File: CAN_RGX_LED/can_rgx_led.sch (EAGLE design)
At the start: 9 parts

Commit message: board 1_0
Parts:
- added R1: 22M, SparkFun-Resistors:22MOHM-0603-1/10W-10%
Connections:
- new net N$8: R1.1, U$1.A
- net +: now also R1.2; no longer U$1.A
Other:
- moved on the sheet: U$1, U$2, U$3, U$4, U$5, U$6, U$7, U$8
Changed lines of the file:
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@@
 <part name="U$8" library="uORocketry-parts" deviceset="OSLONSSL150" device=""/>
 <part name="J1" library="SparkFun-Connectors" deviceset="CONN_02" device=""/>
+<part name="R1" library="SparkFun-Resistors" deviceset="22MOHM" device="-0603-1/10W-10%" value="22M"/>
 </parts>
 <sheets>
@@
 </plain>
 <instances>
-<instance part="U$1" gate="G$1" x="33.02" y="55.88" smashed="yes">
-<attribute name="NAME" x="32.512" y="52.451" size="1.778" layer="95" font="vector" rot="R180"/>
-<attribute name="VALUE" x="32.512" y="57.785" size="1.778" layer="96" font="vector" rot="R180" align="top-left"/>
-</instance>
-<instance part="U$2" gate="G$1" x="48.26" y="55.88" smashed="yes">
+<instance part="U$1" gate="G$1" x="48.26" y="55.88" smashed="yes">
 <attribute name="NAME" x="47.752" y="52.451" size="1.778" layer="95" font="vector" rot="R180"/>
 <attribute name="VALUE" x="47.752" y="57.785" size="1.778" layer="96" font="vector" rot="R180" align="top-left"/>
 </instance>
-<instance part="U$3" gate="G$1" x="63.5" y="55.88" smashed="yes">
+<instance part="U$2" gate="G$1" x="63.5" y="55.88" smashed="yes">
 <attribute name="NAME" x="62.992" y="52.451" size="1.778" layer="95" font="vector" rot="R180"/>
 <attribute name="VALUE" x="62.992" y="57.785" size="1.778" layer="96" font="vector" rot="R180" align="top-left"/>
 </instance>
-<instance part="U$4" gate="G$1" x="76.2" y="55.88" smashed="yes">
-<attribute name="NAME" x="75.692" y="52.451" size="1.778" layer="95" font="vector" rot="R180"/>
-<attribute name="VALUE" x="75.692" y="57.785" size="1.778" layer="96" font="vector" rot="R180" align="top-left"/>
+<instance part="U$3" gate="G$1" x="78.74" y="55.88" smashed="yes">
+<attribute name="NAME" x="78.232" y="52.451" size="1.778" layer="95" font="vector" rot="R180"/>
+<attribute name="VALUE" x="78.232" y="57.785" size="1.778" layer="96" font="vector" rot="R180" align="top-left"/>
 </instance>
-<instance part="U$5" gate="G$1" x="33.02" y="40.64" smashed="yes">
-<attribute name="NAME" x="32.512" y="37.211" size="1.778" layer="95" font="vector" rot="R180"/>
-<attribute name="VALUE" x="32.512" y="42.545" size="1.778" layer="96" font="vector" rot="R180" align="top-left"/>
+<instance part="U$4" gate="G$1" x="91.44" y="55.88" smashed="yes">
+<attribute name="NAME" x="90.932" y="52.451" size="1.778" layer="95" font="vector" rot="R180"/>
+<attribute name="VALUE" x="90.932" y="57.785" size="1.778" layer="96" font="vector" rot="R180" align="top-left"/>
 </instance>
-<instance part="U$6" gate="G$1" x="48.26" y="40.64" smashed="yes">
+<instance part="U$5" gate="G$1" x="48.26" y="40.64" smashed="yes">
 <attribute name="NAME" x="47.752" y="37.211" size="1.778" layer="95" font="vector" rot="R180"/>
 <attribute name="VALUE" x="47.752" y="42.545" size="1.778" layer="96" font="vector" rot="R180" align="top-left"/>
 </instance>
-<instance part="U$7" gate="G$1" x="63.5" y="40.64" smashed="yes">
+<instance part="U$6" gate="G$1" x="63.5" y="40.64" smashed="yes">
 <attribute name="NAME" x="62.992" y="37.211" size="1.778" layer="95" font="vector" rot="R180"/>
 <attribute name="VALUE" x="62.992" y="42.545" size="1.778" layer="96" font="vector" rot="R180" align="top-left"/>
 </instance>
-<instance part="U$8" gate="G$1" x="78.74" y="40.64" smashed="yes">
+<instance part="U$7" gate="G$1" x="78.74" y="40.64" smashed="yes">
 <attribute name="NAME" x="78.232" y="37.211" size="1.778" layer="95" font="vector" rot="R180"/>
 <attribute name="VALUE" x="78.232" y="42.545" size="1.778" layer="96" font="vector" rot="R180" align="top-left"/>
+</instance>
+<instance part="U$8" gate="G$1" x="93.98" y="40.64" smashed="yes">
+<attribute name="NAME" x="93.472" y="37.211" size="1.778" layer="95" font="vector" rot="R180"/>
+<attribute name="VALUE" x="93.472" y="42.545" size="1.778" layer="96" font="vector" rot="R180" align="top-left"/>
 </instance>
 <instance part="J1" gate="G$1" x="17.78" y="68.58" smashed="yes">
 <attribute name="VALUE" x="15.24" y="63.754" size="1.778" layer="96" font="vector"/>
 <attribute name="NAME" x="15.24" y="74.168" size="1.778" layer="95" font="vector"/>
+</instance>
+<instance part="R1" gate="G$1" x="33.02" y="55.88" smashed="yes" rot="R180">
+<attribute name="NAME" x="33.02" y="54.356" size="1.778" layer="95" font="vector" rot="R180" align="bottom-center"/>
+<attribute name="VALUE" x="33.02" y="57.404" size="1.778" layer="96" font="vector" rot="R180" align="top-center"/>
 </instance>
 </instances>
@@
 <pinref part="U$1" gate="G$1" pin="C"/>
 <pinref part="U$2" gate="G$1" pin="A"/>
-<wire x1="33.02" y1="55.88" x2="40.64" y2="55.88" width="0.1524" layer="91"/>
+<wire x1="48.26" y1="55.88" x2="55.88" y2="55.88" width="0.1524" layer="91"/>
 </segment>
 </net>
@@
 <pinref part="U$2" gate="G$1" pin="C"/>
 <pinref part="U$3" gate="G$1" pin="A"/>
-<wire x1="48.26" y1="55.88" x2="55.88" y2="55.88" width="0.1524" layer="91"/>
+<wire x1="63.5" y1="55.88" x2="71.12" y2="55.88" width="0.1524" layer="91"/>
 </segment>
 </net>
@@
 <pinref part="U$3" gate="G$1" pin="C"/>
 <pinref part="U$4" gate="G$1" pin="A"/>
-<wire x1="63.5" y1="55.88" x2="68.58" y2="55.88" width="0.1524" layer="91"/>
+<wire x1="78.74" y1="55.88" x2="83.82" y2="55.88" width="0.1524" layer="91"/>
 </segment>
 </net>
@@
 <segment>
 <pinref part="U$4" gate="G$1" pin="C"/>
-<wire x1="76.2" y1="55.88" x2="76.2" y2="48.26" width="0.1524" layer="91"/>
-<wire x1="76.2" y1="48.26" x2="25.4" y2="48.26" width="0.1524" layer="91"/>
+<wire x1="91.44" y1="55.88" x2="91.44" y2="48.26" width="0.1524" layer="91"/>
+<wire x1="91.44" y1="48.26" x2="40.64" y2="48.26" width="0.1524" layer="91"/>
 <pinref part="U$5" gate="G$1" pin="A"/>
-<wire x1="25.4" y1="48.26" x2="25.4" y2="40.64" width="0.1524" layer="91"/>
+<wire x1="40.64" y1="48.26" x2="40.64" y2="40.64" width="0.1524" layer="91"/>
 </segment>
 </net>
@@
 <pinref part="U$5" gate="G$1" pin="C"/>
 <pinref part="U$6" gate="G$1" pin="A"/>
-<wire x1="33.02" y1="40.64" x2="40.64" y2="40.64" width="0.1524" layer="91"/>
+<wire x1="48.26" y1="40.64" x2="55.88" y2="40.64" width="0.1524" layer="91"/>
 </segment>
 </net>
@@
 <pinref part="U$6" gate="G$1" pin="C"/>
 <pinref part="U$7" gate="G$1" pin="A"/>
-<wire x1="48.26" y1="40.64" x2="55.88" y2="40.64" width="0.1524" layer="91"/>
+<wire x1="63.5" y1="40.64" x2="71.12" y2="40.64" width="0.1524" layer="91"/>
 </segment>
 </net>
@@
 <pinref part="U$7" gate="G$1" pin="C"/>
 <pinref part="U$8" gate="G$1" pin="A"/>
-<wire x1="63.5" y1="40.64" x2="71.12" y2="40.64" width="0.1524" layer="91"/>
-</segment>
-</net>
-<net name="+" class="0">
-<segment>
-<pinref part="J1" gate="G$1" pin="1"/>
-<pinref part="U$1" gate="G$1" pin="A"/>
-<wire x1="25.4" y1="68.58" x2="25.4" y2="55.88" width="0.1524" layer="91"/>
-<label x="27.94" y="63.5" size="1.778" layer="95"/>
+<wire x1="78.74" y1="40.64" x2="86.36" y2="40.64" width="0.1524" layer="91"/>
 </segment>
 </net>
@@
 <pinref part="J1" gate="G$1" pin="2"/>
 <pinref part="U$8" gate="G$1" pin="C"/>
-<wire x1="25.4" y1="71.12" x2="78.74" y2="71.12" width="0.1524" layer="91"/>
-<wire x1="78.74" y1="71.12" x2="78.74" y2="40.64" width="0.1524" layer="91"/>
-<label x="25.4" y="71.12" size="1.778" layer="95"/>
+<wire x1="25.4" y1="71.12" x2="93.98" y2="71.12" width="0.1524" layer="91"/>
+<wire x1="93.98" y1="71.12" x2="93.98" y2="40.64" width="0.1524" layer="91"/>
+<label x="40.64" y="71.12" size="1.778" layer="95"/>
 </segment>
 </net>
+<net name="N$8" class="0">
+<segment>
+<pinref part="R1" gate="G$1" pin="1"/>
+<pinref part="U$1" gate="G$1" pin="A"/>
+<wire x1="38.1" y1="55.88" x2="40.64" y2="55.88" width="0.1524" layer="91"/>
+</segment>
+</net>
+<net name="+" class="0">
+<segment>
+<pinref part="R1" gate="G$1" pin="2"/>
+<pinref part="J1" gate="G$1" pin="1"/>
+<wire x1="27.94" y1="55.88" x2="27.94" y2="68.58" width="0.1524" layer="91"/>
+<wire x1="27.94" y1="68.58" x2="25.4" y2="68.58" width="0.1524" layer="91"/>
+</segment>
+</net>

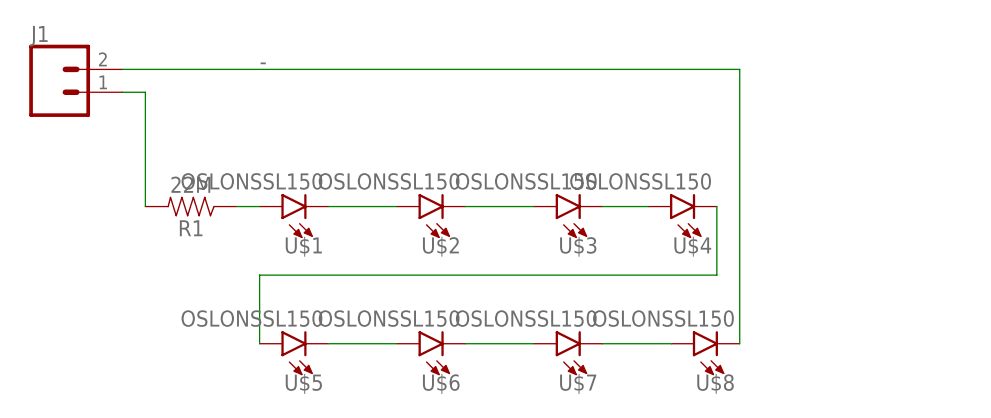
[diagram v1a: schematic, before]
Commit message: switch LED package
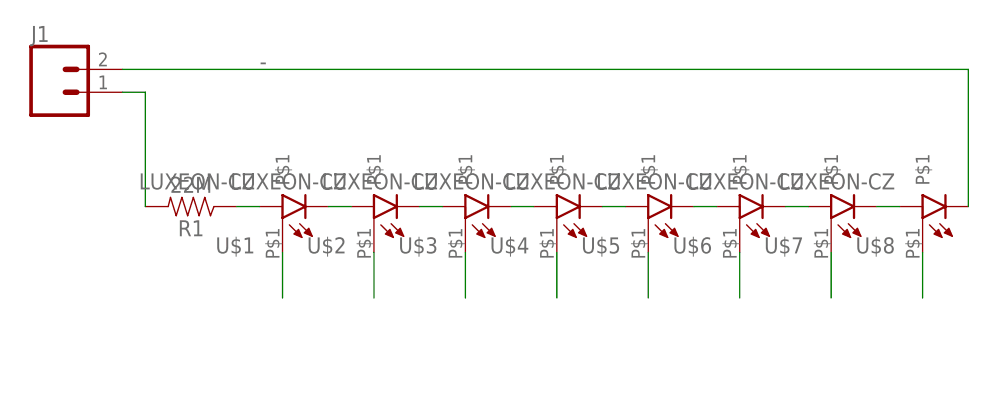
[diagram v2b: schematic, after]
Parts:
- U$1, U$2, U$3, U$4, U$5, U$6, U$7, U$8: value OSLONSSL150 -> LUXEON-CZ; device uORocketry-parts:OSLONSSL150 -> uORocketry-parts:LUXEON-CZ
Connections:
- new net N$1: U$3.P$1
- new net N$16: U$1.P$1
- new net N$17: U$2.P$1
- new net N$19: U$4.P$1
- new net N$20: U$5.P$1
- new net N$21: U$6.P$1
- new net N$22: U$7.P$1
- new net N$23: U$8.P$1

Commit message: connect middle to anodes as suggested by ayman
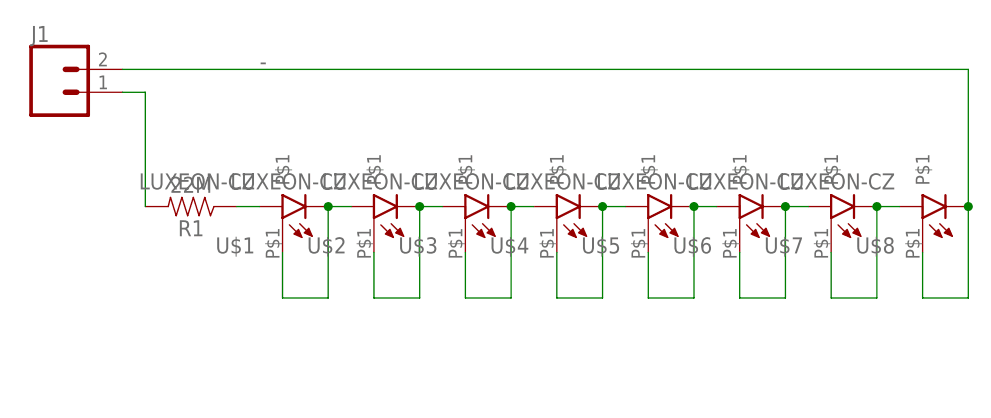
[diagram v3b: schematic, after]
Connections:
- removed net N$10: U$2.C, U$3.A
- removed net N$11: U$3.C, U$4.A
- removed net N$12: U$4.C, U$5.A
- removed net N$13: U$5.C, U$6.A
- removed net N$14: U$6.C, U$7.A
- removed net N$15: U$7.C, U$8.A
- removed net N$23: U$8.P$1
- removed net N$9: U$1.C, U$2.A
- net -: now also U$8.P$1
- net N$1: now also U$3.C, U$4.A
- net N$16: now also U$1.C, U$2.A
- net N$17: now also U$2.C, U$3.A
- net N$19: now also U$4.C, U$5.A
- net N$20: now also U$5.C, U$6.A
- net N$21: now also U$6.C, U$7.A
- net N$22: now also U$7.C, U$8.A
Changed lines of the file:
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@@
 <?xml version="1.0" encoding="utf-8"?>
 <!DOCTYPE eagle SYSTEM "eagle.dtd">
-<eagle version="9.5.2">
+<eagle version="9.4.2">
 <drawing>
 <settings>
@@
 <pinref part="U$8" gate="G$1" pin="C"/>
 <wire x1="119.38" y1="55.88" x2="119.38" y2="71.12" width="0.1524" layer="91"/>
+<pinref part="U$8" gate="G$1" pin="P$1"/>
+<wire x1="114.3" y1="50.8" x2="114.3" y2="45.72" width="0.1524" layer="91"/>
+<wire x1="114.3" y1="45.72" x2="119.38" y2="45.72" width="0.1524" layer="91"/>
+<wire x1="119.38" y1="45.72" x2="119.38" y2="55.88" width="0.1524" layer="91"/>
+<junction x="119.38" y="55.88"/>
 </segment>
 </net>
@@
 </segment>
 </net>
-<net name="N$9" class="0">
-<segment>
+<net name="N$16" class="0">
+<segment>
+<pinref part="U$1" gate="G$1" pin="P$1"/>
+<wire x1="43.18" y1="50.8" x2="43.18" y2="45.72" width="0.1524" layer="91"/>
 <pinref part="U$1" gate="G$1" pin="C"/>
 <pinref part="U$2" gate="G$1" pin="A"/>
 <wire x1="48.26" y1="55.88" x2="50.8" y2="55.88" width="0.1524" layer="91"/>
-</segment>
-</net>
-<net name="N$10" class="0">
-<segment>
+<wire x1="43.18" y1="45.72" x2="48.26" y2="45.72" width="0.1524" layer="91"/>
+<wire x1="48.26" y1="45.72" x2="48.26" y2="55.88" width="0.1524" layer="91"/>
+<junction x="48.26" y="55.88"/>
+</segment>
+</net>
+<net name="N$17" class="0">
+<segment>
+<pinref part="U$2" gate="G$1" pin="P$1"/>
+<wire x1="53.34" y1="50.8" x2="53.34" y2="45.72" width="0.1524" layer="91"/>
 <pinref part="U$2" gate="G$1" pin="C"/>
 <pinref part="U$3" gate="G$1" pin="A"/>
 <wire x1="58.42" y1="55.88" x2="60.96" y2="55.88" width="0.1524" layer="91"/>
-</segment>
-</net>
-<net name="N$11" class="0">
-<segment>
+<wire x1="53.34" y1="45.72" x2="58.42" y2="45.72" width="0.1524" layer="91"/>
+<wire x1="58.42" y1="45.72" x2="58.42" y2="55.88" width="0.1524" layer="91"/>
+<junction x="58.42" y="55.88"/>
+</segment>
+</net>
+<net name="N$1" class="0">
+<segment>
+<pinref part="U$3" gate="G$1" pin="P$1"/>
+<wire x1="63.5" y1="50.8" x2="63.5" y2="45.72" width="0.1524" layer="91"/>
 <pinref part="U$3" gate="G$1" pin="C"/>
 <pinref part="U$4" gate="G$1" pin="A"/>
 <wire x1="68.58" y1="55.88" x2="71.12" y2="55.88" width="0.1524" layer="91"/>
-</segment>
-</net>
-<net name="N$12" class="0">
-<segment>
+<wire x1="63.5" y1="45.72" x2="68.58" y2="45.72" width="0.1524" layer="91"/>
+<wire x1="68.58" y1="45.72" x2="68.58" y2="55.88" width="0.1524" layer="91"/>
+<junction x="68.58" y="55.88"/>
+</segment>
+</net>
+<net name="N$19" class="0">
+<segment>
+<pinref part="U$4" gate="G$1" pin="P$1"/>
+<wire x1="73.66" y1="50.8" x2="73.66" y2="45.72" width="0.1524" layer="91"/>
 <pinref part="U$4" gate="G$1" pin="C"/>
 <pinref part="U$5" gate="G$1" pin="A"/>
 <wire x1="78.74" y1="55.88" x2="81.28" y2="55.88" width="0.1524" layer="91"/>
-</segment>
-</net>
-<net name="N$13" class="0">
-<segment>
+<wire x1="73.66" y1="45.72" x2="78.74" y2="45.72" width="0.1524" layer="91"/>
+<wire x1="78.74" y1="45.72" x2="78.74" y2="55.88" width="0.1524" layer="91"/>
+<junction x="78.74" y="55.88"/>
+</segment>
+</net>
+<net name="N$20" class="0">
+<segment>
+<pinref part="U$5" gate="G$1" pin="P$1"/>
+<wire x1="83.82" y1="50.8" x2="83.82" y2="45.72" width="0.1524" layer="91"/>
 <pinref part="U$5" gate="G$1" pin="C"/>
 <pinref part="U$6" gate="G$1" pin="A"/>
 <wire x1="88.9" y1="55.88" x2="91.44" y2="55.88" width="0.1524" layer="91"/>
-</segment>
-</net>
-<net name="N$14" class="0">
-<segment>
+<wire x1="83.82" y1="45.72" x2="88.9" y2="45.72" width="0.1524" layer="91"/>
+<wire x1="88.9" y1="45.72" x2="88.9" y2="55.88" width="0.1524" layer="91"/>
+<junction x="88.9" y="55.88"/>
+</segment>
+</net>
+<net name="N$21" class="0">
+<segment>
+<pinref part="U$6" gate="G$1" pin="P$1"/>
+<wire x1="93.98" y1="50.8" x2="93.98" y2="45.72" width="0.1524" layer="91"/>
 <pinref part="U$6" gate="G$1" pin="C"/>
 <pinref part="U$7" gate="G$1" pin="A"/>
 <wire x1="99.06" y1="55.88" x2="101.6" y2="55.88" width="0.1524" layer="91"/>
-</segment>
-</net>
-<net name="N$15" class="0">
-<segment>
+<wire x1="93.98" y1="45.72" x2="99.06" y2="45.72" width="0.1524" layer="91"/>
+<wire x1="99.06" y1="45.72" x2="99.06" y2="55.88" width="0.1524" layer="91"/>
+<junction x="99.06" y="55.88"/>
+</segment>
+</net>
+<net name="N$22" class="0">
+<segment>
+<pinref part="U$7" gate="G$1" pin="P$1"/>
+<wire x1="104.14" y1="50.8" x2="104.14" y2="45.72" width="0.1524" layer="91"/>
 <pinref part="U$7" gate="G$1" pin="C"/>
 <pinref part="U$8" gate="G$1" pin="A"/>
 <wire x1="109.22" y1="55.88" x2="111.76" y2="55.88" width="0.1524" layer="91"/>
-</segment>
-</net>
-<net name="N$16" class="0">
-<segment>
-<pinref part="U$1" gate="G$1" pin="P$1"/>
-<wire x1="43.18" y1="50.8" x2="43.18" y2="45.72" width="0.1524" layer="91"/>
-</segment>
-</net>
-<net name="N$17" class="0">
-<segment>
-<pinref part="U$2" gate="G$1" pin="P$1"/>
-<wire x1="53.34" y1="50.8" x2="53.34" y2="45.72" width="0.1524" layer="91"/>
-</segment>
-</net>
-<net name="N$1" class="0">
-<segment>
-<pinref part="U$3" gate="G$1" pin="P$1"/>
-<wire x1="63.5" y1="50.8" x2="63.5" y2="45.72" width="0.1524" layer="91"/>
-</segment>
-</net>
-<net name="N$19" class="0">
-<segment>
-<pinref part="U$4" gate="G$1" pin="P$1"/>
-<wire x1="73.66" y1="50.8" x2="73.66" y2="45.72" width="0.1524" layer="91"/>
-</segment>
-</net>
-<net name="N$20" class="0">
-<segment>
-<pinref part="U$5" gate="G$1" pin="P$1"/>
-<wire x1="83.82" y1="50.8" x2="83.82" y2="45.72" width="0.1524" layer="91"/>
-</segment>
-</net>
-<net name="N$21" class="0">
-<segment>
-<pinref part="U$6" gate="G$1" pin="P$1"/>
-<wire x1="93.98" y1="50.8" x2="93.98" y2="45.72" width="0.1524" layer="91"/>
-</segment>
-</net>
-<net name="N$22" class="0">
-<segment>
-<pinref part="U$7" gate="G$1" pin="P$1"/>
-<wire x1="104.14" y1="50.8" x2="104.14" y2="45.72" width="0.1524" layer="91"/>
-</segment>
-</net>
-<net name="N$23" class="0">
-<segment>
-<pinref part="U$8" gate="G$1" pin="P$1"/>
-<wire x1="114.3" y1="50.8" x2="114.3" y2="45.72" width="0.1524" layer="91"/>
-</segment>
-</net>
+<wire x1="104.14" y1="45.72" x2="109.22" y2="45.72" width="0.1524" layer="91"/>
+<wire x1="109.22" y1="45.72" x2="109.22" y2="55.88" width="0.1524" layer="91"/>
+<junction x="109.22" y="55.88"/>
+</segment>
+</net>
